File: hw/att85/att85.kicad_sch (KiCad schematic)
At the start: 42 parts, among them J101 Barrel_Jack_Switch, J102 Screw_Terminal_01x03, J103 AVR-ISP-6, J104 Conn_01x02, J105 Conn_01x02, Q101 BC817, SW101 SW_Push, SW102 SW_Push, SW103 SW_Push, SW104 SW_Push, SW105 SW_Push, SW106 SW_Push, U101 ATtiny85-20P, U102 MT3608-MODULE, U105 74AHC1G125

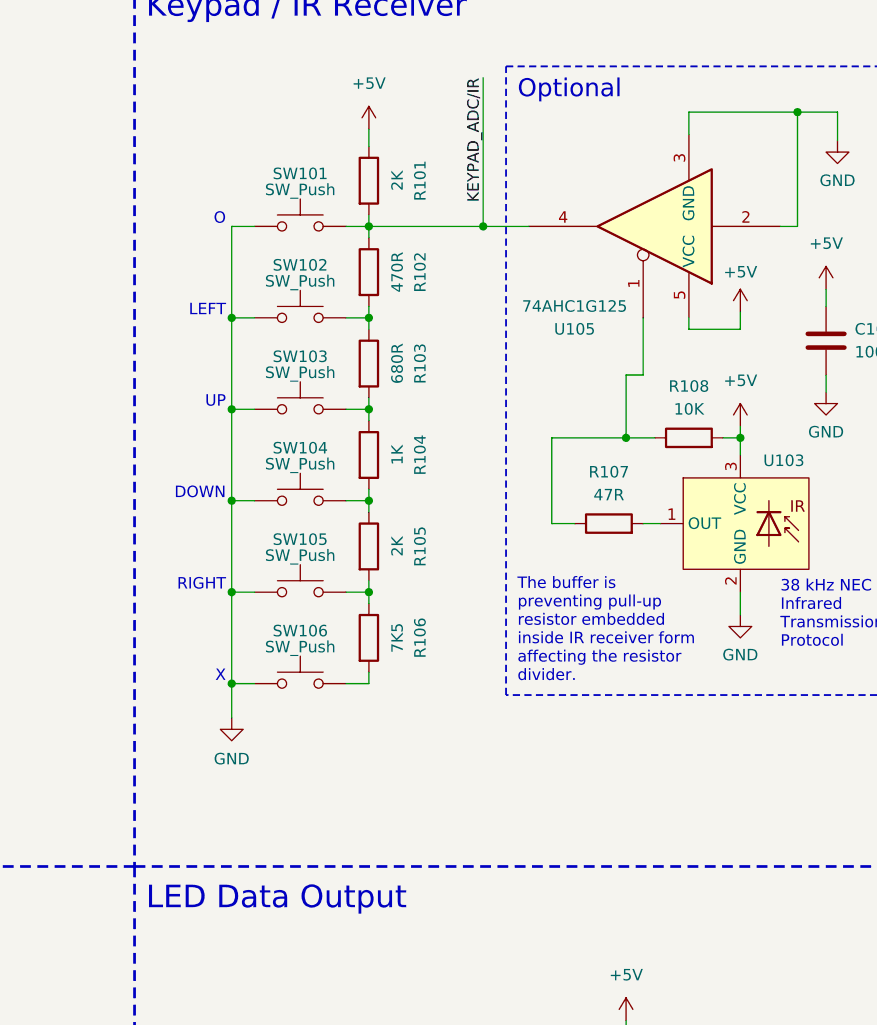
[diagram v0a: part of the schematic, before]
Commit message: chore(hw): add separate divider position for IR receiver
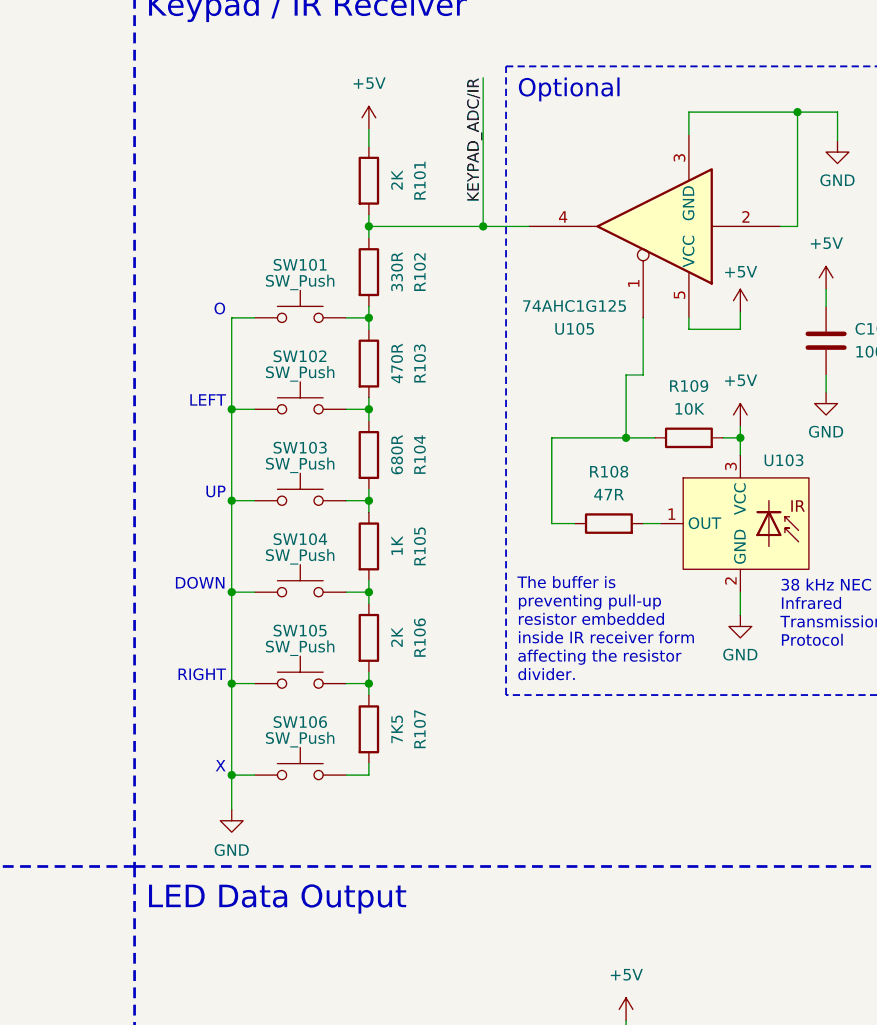
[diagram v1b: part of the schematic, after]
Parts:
- added R102: 330R, Resistor_SMD:R_0805_2012Metric_Pad1.20x1.40mm_HandSolder, symbol Device:R
- renumbered R102 to R103, R103 to R104, R104 to R105, R105 to R106, R106 to R107, R107 to R108, R108 to R109
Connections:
- net KEYPAD_ADC/IR: now also R102.1; no longer R103.1, SW101.2
- new net: R102.2, R103.1, SW101.2
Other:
- moved on the sheet: R103, R104, R105, R106, R107, SW101, SW102, SW103, SW104, SW105, SW106

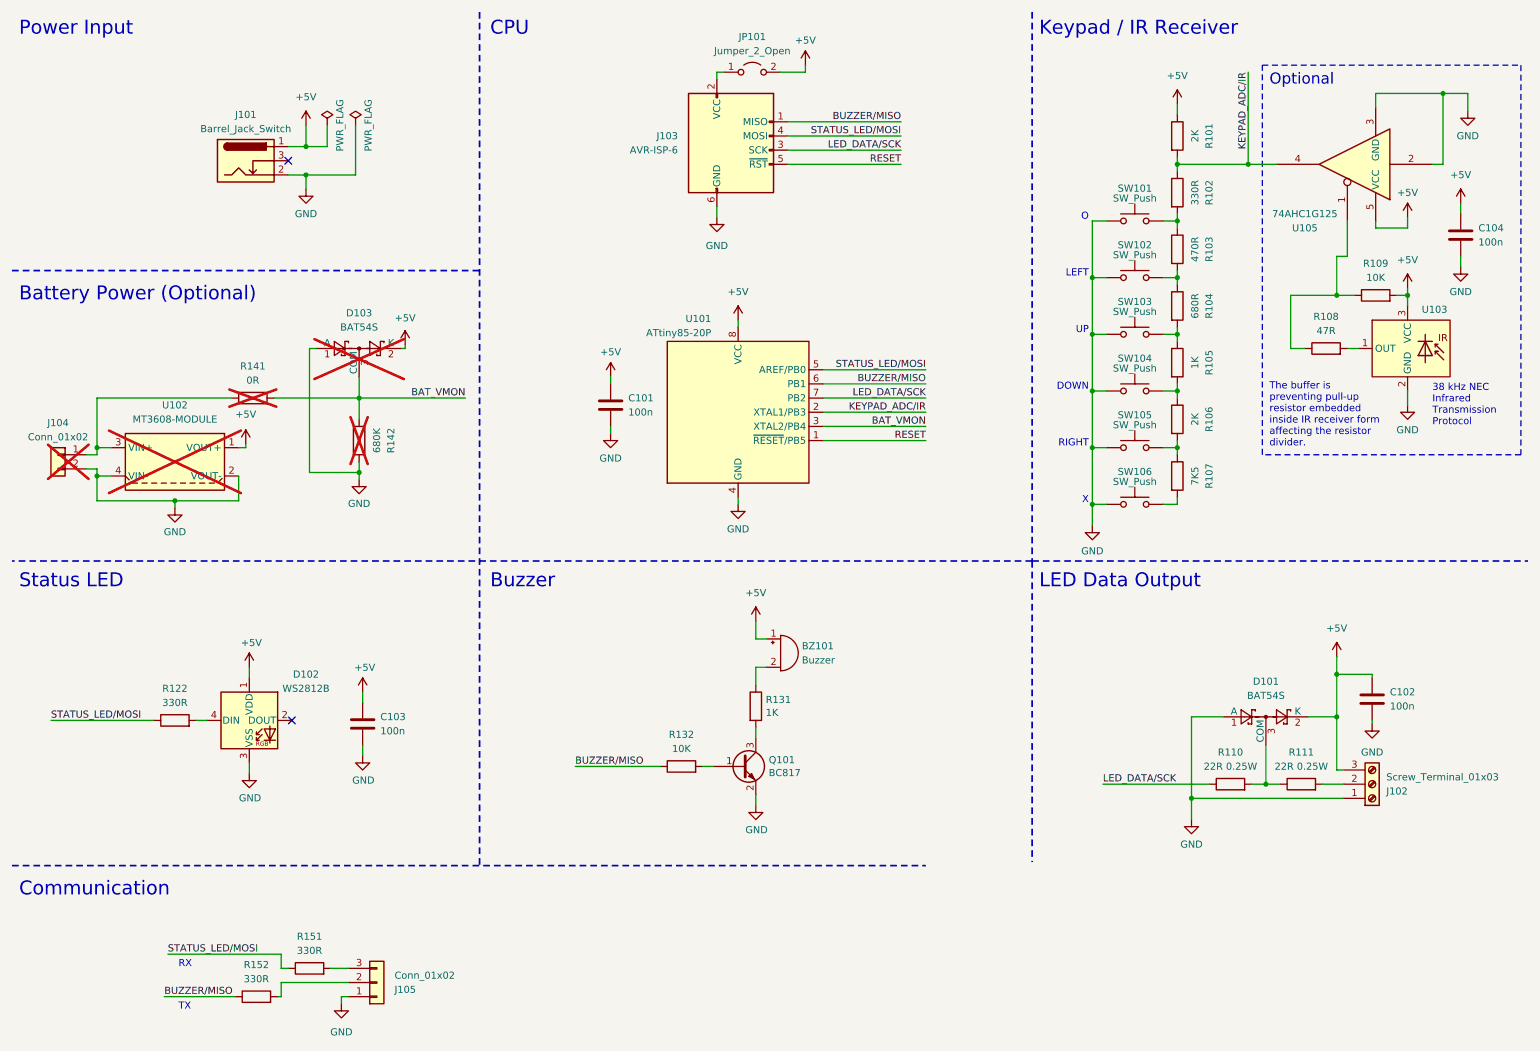
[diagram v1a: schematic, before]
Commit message: chore(hw): remove UART RX, allow buzzer to be disconnected
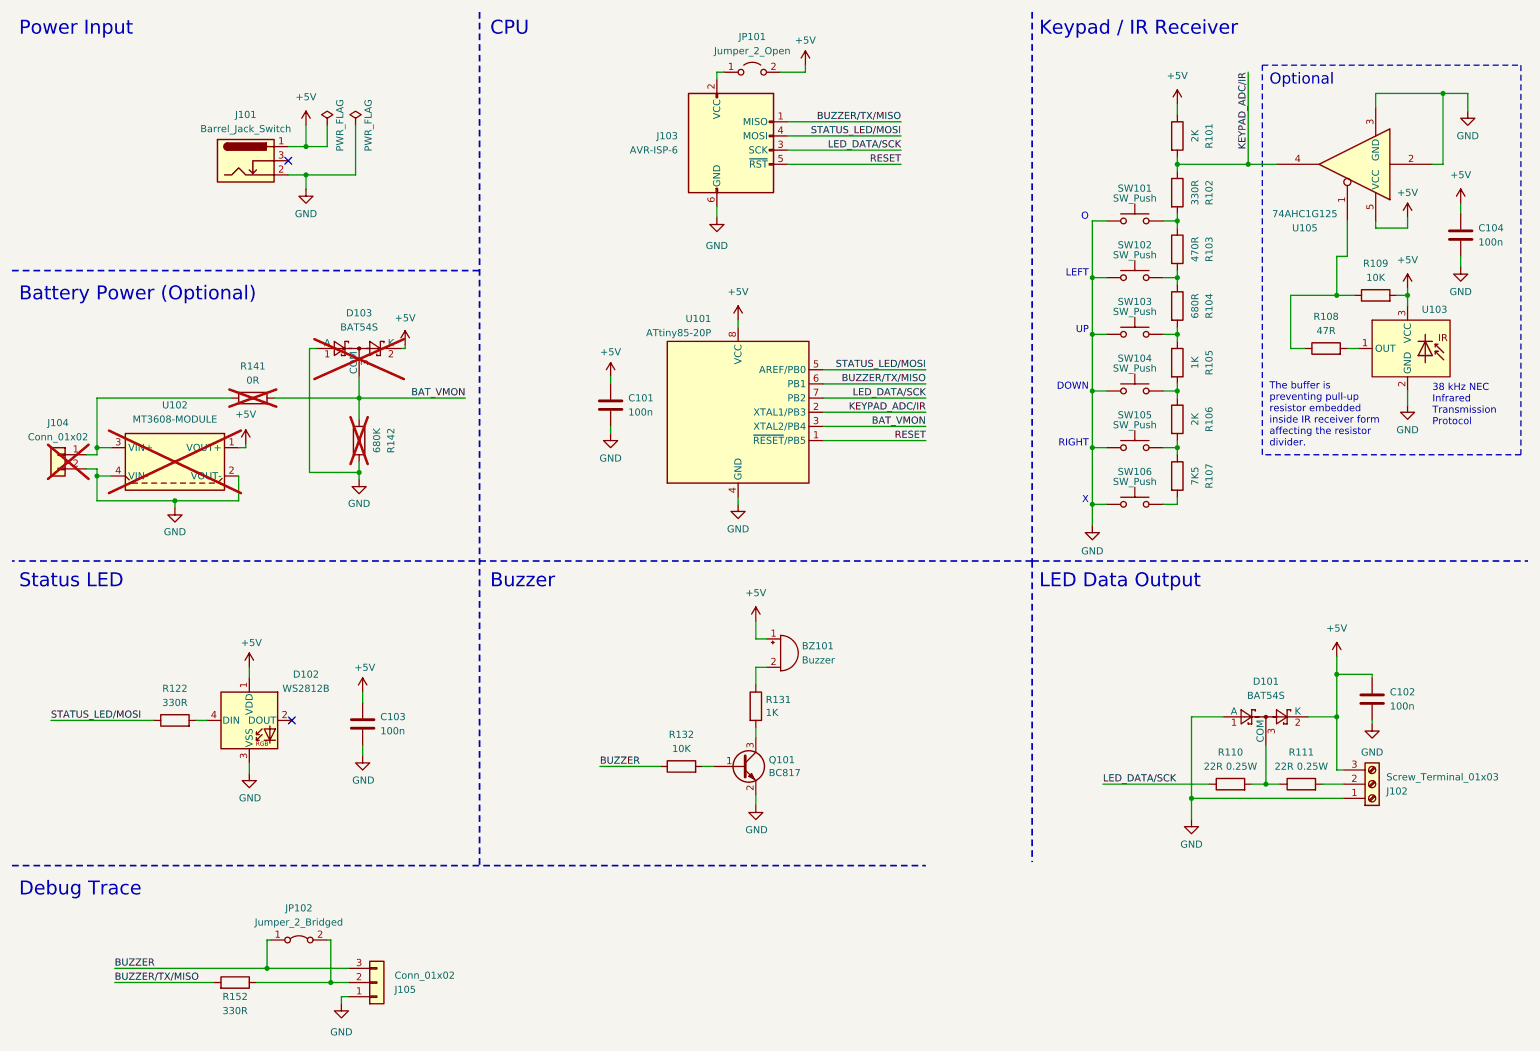
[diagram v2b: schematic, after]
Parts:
- removed R151: 330R, Resistor_SMD:R_0805_2012Metric_Pad1.20x1.40mm_HandSolder, symbol Device:R
- added JP102: Jumper_2_Bridged, Jumper:SolderJumper-2_P1.3mm_Bridged_RoundedPad1.0x1.5mm, symbol Jumper:Jumper_2_Bridged
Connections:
- net BUZZER: now reaches J105.3 (Pin_3)
- net BUZZER: now also R132.1, JP102.1 (A)
- net at J105.2 (Pin_2): now also R152.1, JP102.2 (B); no longer R152.2
- net BUZZER/MISO renamed BUZZER/TX/MISO
- net BUZZER/TX/MISO: now also R152.2; no longer R132.1, R152.1
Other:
- note added: "Debug Trace"
- note removed: "Communication"
- note removed: "RX"
- note removed: "TX"
- moved on the sheet: R152
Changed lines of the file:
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@@
     (comment 1 "www.stefanmisik.com")
   )
+  (junction (at 69.85 186.69) (diameter 0) (color 0 0 0 0)
+  )
   (junction (at 237.49 151.13) (diameter 0) (color 0 0 0 0)
   )
@@
   )
   (junction (at 206.375 80.645) (diameter 0) (color 0 0 0 0)
+  )
+  (junction (at 58.42 184.15) (diameter 0) (color 0 0 0 0)
   )
   (junction (at 269.24 27.305) (diameter 0) (color 0 0 0 0)
@@
     (stroke (width 0) (type default))
   )
+  (wire (pts (xy 69.85 179.07) (xy 69.85 186.69))
+    (stroke (width 0) (type default))
+  )
   (wire (pts (xy 245.11 139.065) (xy 250.19 139.065))
     (stroke (width 0) (type default))
@@
     (stroke (width 0) (type default))
   )
-  (wire (pts (xy 113.665 147.955) (xy 128.905 147.955))
-    (stroke (width 0) (type default))
-  )
-  (wire (pts (xy 60.96 189.23) (xy 60.96 186.69))
+  (wire (pts (xy 118.11 147.955) (xy 128.905 147.955))
     (stroke (width 0) (type default))
   )
@@
     (stroke (width 0) (type default))
   )
+  (wire (pts (xy 69.85 186.69) (xy 73.025 186.69))
+    (stroke (width 0) (type default))
+  )
   (wire (pts (xy 221.615 100.965) (xy 221.615 99.695))
     (stroke (width 0) (type default))
@@
   )
   (wire (pts (xy 221.615 40.005) (xy 234.315 40.005))
-    (stroke (width 0) (type default))
-  )
-  (wire (pts (xy 69.85 184.15) (xy 73.025 184.15))
     (stroke (width 0) (type default))
   )
@@
     (stroke (width 0) (type default))
   )
-  (wire (pts (xy 40.64 181.61) (xy 60.96 181.61))
-    (stroke (width 0) (type default))
-  )
   (polyline (pts (xy 195.58 12.7) (xy 195.58 111.125))
     (stroke (width 0.3) (type dash))
@@
     (stroke (width 0) (type default))
   )
-  (wire (pts (xy 60.96 186.69) (xy 73.025 186.69))
+  (wire (pts (xy 56.515 186.69) (xy 69.85 186.69))
     (stroke (width 0) (type default))
   )
@@
     (stroke (width 0) (type default))
   )
+  (wire (pts (xy 58.42 184.15) (xy 73.025 184.15))
+    (stroke (width 0) (type default))
+  )
   (wire (pts (xy 221.615 41.275) (xy 221.615 40.005))
     (stroke (width 0) (type default))
@@
   )
   (wire (pts (xy 27.94 95.885) (xy 30.48 95.885))
+    (stroke (width 0) (type default))
+  )
+  (wire (pts (xy 58.42 179.07) (xy 58.42 184.15))
     (stroke (width 0) (type default))
   )
@@
     (stroke (width 0) (type default))
   )
-  (wire (pts (xy 60.325 189.23) (xy 60.96 189.23))
-    (stroke (width 0) (type default))
-  )
   (wire (pts (xy 66.04 95.25) (xy 74.93 95.25))
     (stroke (width 0) (type default))
@@
     (stroke (width 0) (type default))
   )
-  (wire (pts (xy 40.005 189.23) (xy 52.705 189.23))
+  (wire (pts (xy 31.115 186.69) (xy 48.895 186.69))
     (stroke (width 0) (type default))
   )
@@
   )
   (wire (pts (xy 74.93 95.25) (xy 74.93 96.52))
-    (stroke (width 0) (type default))
-  )
-  (wire (pts (xy 60.96 184.15) (xy 60.96 181.61))
     (stroke (width 0) (type default))
   )
@@
     (stroke (width 0) (type default))
   )
+  (wire (pts (xy 69.215 179.07) (xy 69.85 179.07))
+    (stroke (width 0) (type default))
+  )
   (wire (pts (xy 206.375 70.485) (xy 208.915 70.485))
     (stroke (width 0) (type default))
@@
     (stroke (width 0) (type default))
   )
-  (wire (pts (xy 62.23 184.15) (xy 60.96 184.15))
+  (wire (pts (xy 31.115 184.15) (xy 58.42 184.15))
     (stroke (width 0) (type default))
   )
@@
   )
   (wire (pts (xy 75.565 144.145) (xy 75.565 146.05))
+    (stroke (width 0) (type default))
+  )
+  (wire (pts (xy 59.055 179.07) (xy 58.42 179.07))
     (stroke (width 0) (type default))
   )
@@
     (effects (font (size 1.27 1.27)) (justify right bottom))
   )
-  (text "RX" (at 42.545 184.15 0)
-    (effects (font (size 1.27 1.27)) (justify left bottom))
-  )
   (text "Keypad / IR Receiver" (at 196.85 17.145 0)
     (effects (font (size 2.5 2.5)) (justify left bottom))
@@
     (effects (font (size 1.27 1.27)) (justify right bottom))
   )
-  (text "TX" (at 42.545 191.77 0)
-    (effects (font (size 1.27 1.27)) (justify left bottom))
-  )
   (text "DOWN" (at 205.74 80.645 0)
     (effects (font (size 1.27 1.27)) (justify right bottom))
@@
     (effects (font (size 2.5 2.5)) (justify left bottom))
   )
-  (text "Communication" (at 13.97 171.45 0)
+  (text "Debug Trace" (at 13.97 171.45 0)
     (effects (font (size 2.5 2.5)) (justify left bottom))
   )
@@
     (effects (font (size 1.27 1.27)) (justify left bottom))
   )
-  (label "BUZZER{slash}MISO" (at 172.085 32.385 180) (fields_autoplaced)
+  (label "BUZZER{slash}TX{slash}MISO" (at 172.085 32.385 180) (fields_autoplaced)
     (effects (font (size 1.27 1.27)) (justify right bottom))
   )
@@
     (effects (font (size 1.27 1.27)) (justify right bottom))
   )
-  (label "BUZZER{slash}MISO" (at 40.005 189.23 0) (fields_autoplaced)
+  (label "BUZZER{slash}TX{slash}MISO" (at 31.115 186.69 0) (fields_autoplaced)
     (effects (font (size 1.27 1.27)) (justify left bottom))
   )
@@
     (effects (font (size 1.27 1.27)) (justify right bottom))
   )
+  (label "BUZZER" (at 31.115 184.15 0) (fields_autoplaced)
+    (effects (font (size 1.27 1.27)) (justify left bottom))
+  )
   (label "RESET" (at 176.53 89.535 180) (fields_autoplaced)
     (effects (font (size 1.27 1.27)) (justify right bottom))
@@
     (effects (font (size 1.27 1.27)) (justify right bottom))
   )
-  (label "BUZZER{slash}MISO" (at 176.53 79.375 180) (fields_autoplaced)
+  (label "BUZZER{slash}TX{slash}MISO" (at 176.53 79.375 180) (fields_autoplaced)
     (effects (font (size 1.27 1.27)) (justify right bottom))
   )
-  (label "BUZZER{slash}MISO" (at 113.665 147.955 0) (fields_autoplaced)
+  (label "BUZZER" (at 118.11 147.955 0) (fields_autoplaced)
     (effects (font (size 1.27 1.27)) (justify left bottom))
   )
@@
   (label "KEYPAD_ADC{slash}IR" (at 234.315 23.495 270) (fields_autoplaced)
     (effects (font (size 1.27 1.27)) (justify right bottom))
-  )
-  (label "STATUS_LED{slash}MOSI" (at 40.64 181.61 0) (fields_autoplaced)
-    (effects (font (size 1.27 1.27)) (justify left bottom))
   )
   (label "KEYPAD_ADC{slash}IR" (at 176.53 84.455 180) (fields_autoplaced)
@@
         (path "/fc4ba96f-a9f8-4f1a-a9c5-2b16679a6770"
           (reference "R110") (unit 1)
-        )
-      )
-    )
-  )
-  (symbol (lib_id "Device:R") (at 66.04 184.15 90) (unit 1)
-    (in_bom yes) (on_board yes) (dnp no)
-    (property "Reference" "R151" (at 66.04 178.435 90)
-      (effects (font (size 1.27 1.27)))
-    )
-    (property "Value" "330R" (at 66.04 180.975 90)
-      (effects (font (size 1.27 1.27)))
-    )
-    (property "Footprint" "Resistor_SMD:R_0805_2012Metric_Pad1.20x1.40mm_HandSolder" (at 66.04 185.928 90)
-      (effects (font (size 1.27 1.27)) hide)
-    )
-    (property "Datasheet" "~" (at 66.04 184.15 0)
-      (effects (font (size 1.27 1.27)) hide)
-    )
-    (pin "1")
-    (pin "2")
-    (instances
-      (project "att85"
-        (path "/fc4ba96f-a9f8-4f1a-a9c5-2b16679a6770"
-          (reference "R151") (unit 1)
         )
       )
@@
     )
   )
-  (symbol (lib_id "Device:R") (at 56.515 189.23 90) (unit 1)
-    (in_bom yes) (on_board yes) (dnp no)
-    (property "Reference" "R152" (at 56.515 183.515 90)
-      (effects (font (size 1.27 1.27)))
-    )
-    (property "Value" "330R" (at 56.515 186.055 90)
-      (effects (font (size 1.27 1.27)))
-    )
-    (property "Footprint" "Resistor_SMD:R_0805_2012Metric_Pad1.20x1.40mm_HandSolder" (at 56.515 191.008 90)
-      (effects (font (size 1.27 1.27)) hide)
-    )
-    (property "Datasheet" "~" (at 56.515 189.23 0)
+  (symbol (lib_id "Device:R") (at 52.705 186.69 270) (mirror x) (unit 1)
+    (in_bom yes) (on_board yes) (dnp no)
+    (property "Reference" "R152" (at 52.705 189.23 90)
+      (effects (font (size 1.27 1.27)))
+    )
+    (property "Value" "330R" (at 52.705 191.77 90)
+      (effects (font (size 1.27 1.27)))
+    )
+    (property "Footprint" "Resistor_SMD:R_0805_2012Metric_Pad1.20x1.40mm_HandSolder" (at 52.705 188.468 90)
+      (effects (font (size 1.27 1.27)) hide)
+    )
+    (property "Datasheet" "~" (at 52.705 186.69 0)
       (effects (font (size 1.27 1.27)) hide)
     )
@@
         )
       )
+    )
+  )
+  (symbol (lib_id "Jumper:Jumper_2_Bridged") (at 64.135 179.07 0) (unit 1)
+    (in_bom yes) (on_board yes) (dnp no) (fields_autoplaced)
+    (property "Reference" "JP102" (at 64.135 173.355 0)
+      (effects (font (size 1.27 1.27)))
+    )
+    (property "Value" "Jumper_2_Bridged" (at 64.135 175.895 0)
+      (effects (font (size 1.27 1.27)))
+    )
+    (property "Footprint" "Jumper:SolderJumper-2_P1.3mm_Bridged_RoundedPad1.0x1.5mm" (at 64.135 179.07 0)
+      (effects (font (size 1.27 1.27)) hide)
+    )
+    (property "Datasheet" "~" (at 64.135 179.07 0)
+      (effects (font (size 1.27 1.27)) hide)
+    )
+    (pin "1")
+    (pin "2")
+    (instances
+      (project "att85"
+        (path "/fc4ba96f-a9f8-4f1a-a9c5-2b16679a6770"
+          (reference "JP102") (unit 1)
+        )
+      )

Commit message: refactor(hw): change CPU footprint and 3D model
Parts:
- U101: footprint Package_DIP:DIP-8_W7.62mm -> Package_DIP:DIP-8_W7.62mm_Socket
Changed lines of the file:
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@@
       (effects (font (size 1.27 1.27)) (justify right))
     )
-    (property "Footprint" "Package_DIP:DIP-8_W7.62mm" (at 142.875 84.455 0)
+    (property "Footprint" "Package_DIP:DIP-8_W7.62mm_Socket" (at 142.875 84.455 0)
       (effects (font (size 1.27 1.27) italic) hide)
     )
